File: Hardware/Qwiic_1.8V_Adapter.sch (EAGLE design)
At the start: 18 parts, among them J1 QWIIC_RIGHT_ANGLE, J2 QWIIC_RIGHT_ANGLE, U3 AP2127K-1.8V

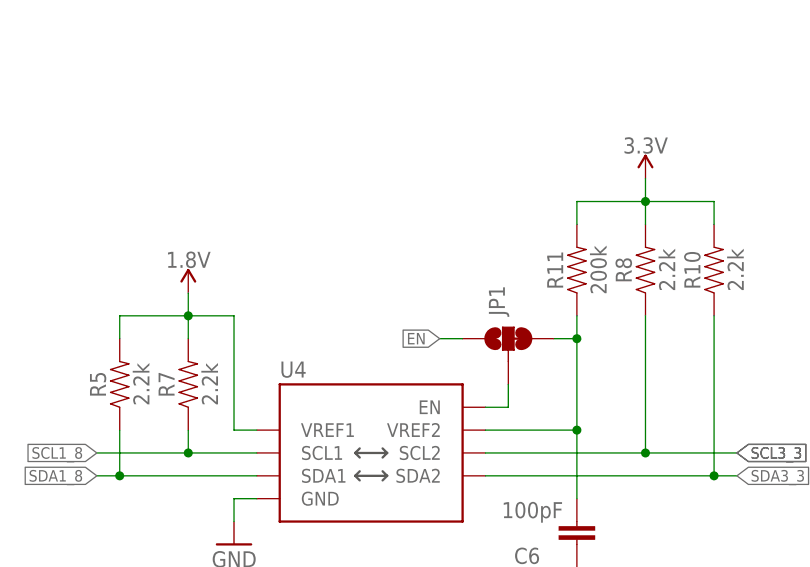
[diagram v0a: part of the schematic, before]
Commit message: Add EN Jumper note
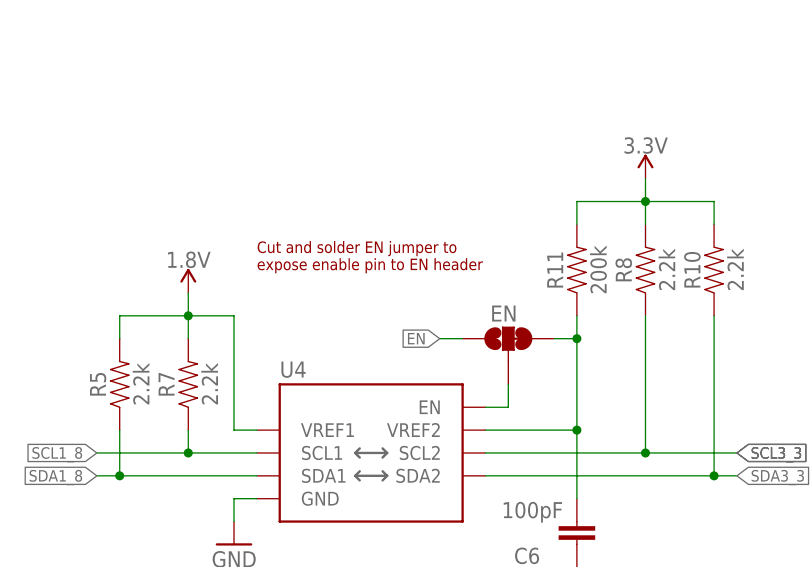
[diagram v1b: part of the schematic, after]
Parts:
- renumbered JP1 to EN
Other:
- note added: "Cut and solder EN jumper to expose enable pin to EN header"
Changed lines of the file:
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@@
 <part name="J4" library="SparkFun-Connectors" deviceset="CONN_05" device="NO_SILK"/>
 <part name="J5" library="SparkFun-Connectors" deviceset="CONN_04" device="1X04_NO_SILK"/>
-<part name="JP1" library="SparkFun-Jumpers" deviceset="JUMPER-SMT_3_1-NC_TRACE" device="_SILK" package3d_urn="urn:adsk.eagle:package:39288/1"/>
+<part name="EN" library="SparkFun-Jumpers" deviceset="JUMPER-SMT_3_1-NC_TRACE" device="_SILK" package3d_urn="urn:adsk.eagle:package:39288/1"/>
 <part name="SUPPLY4" library="SparkFun-PowerSymbols" deviceset="3.3V" device=""/>
 <part name="GND1" library="SparkFun-PowerSymbols" deviceset="GND" device=""/>
@@
 <text x="149.86" y="106.68" size="2.54" layer="97">Qwiic Connectors</text>
 <text x="149.86" y="68.58" size="2.54" layer="97">0.1" Headers</text>
+<text x="55.88" y="111.76" size="1.27" layer="94">Cut and solder EN jumper to
+expose enable pin to EN header</text>
 </plain>
 <instances>
@@
 <attribute name="NAME" x="205.74" y="58.928" size="1.778" layer="95" font="vector"/>
 </instance>
-<instance part="JP1" gate="G$1" x="83.82" y="104.14" smashed="yes" rot="R90">
-<attribute name="NAME" x="83.439" y="106.68" size="1.778" layer="95" font="vector" rot="R90"/>
+<instance part="EN" gate="G$1" x="83.82" y="104.14" smashed="yes" rot="R90">
+<attribute name="NAME" x="84.836" y="107.823" size="1.778" layer="95" font="vector" rot="R180"/>
 </instance>
 <instance part="SUPPLY4" gate="G$1" x="185.42" y="99.06" smashed="yes">
@@
 <wire x1="91.44" y1="93.98" x2="91.44" y2="86.36" width="0.1524" layer="91"/>
 <junction x="91.44" y="93.98"/>
-<pinref part="JP1" gate="G$1" pin="3"/>
+<pinref part="EN" gate="G$1" pin="3"/>
 <wire x1="88.9" y1="104.14" x2="91.44" y2="104.14" width="0.1524" layer="91"/>
 <junction x="91.44" y="104.14"/>
@@
 <segment>
 <pinref part="U4" gate="G$1" pin="EN"/>
-<pinref part="JP1" gate="G$1" pin="2"/>
+<pinref part="EN" gate="G$1" pin="2"/>
 <wire x1="81.28" y1="96.52" x2="83.82" y2="96.52" width="0.1524" layer="91"/>
 <wire x1="83.82" y1="96.52" x2="83.82" y2="99.06" width="0.1524" layer="91"/>
@@
 <net name="EN" class="0">
 <segment>
-<pinref part="JP1" gate="G$1" pin="1"/>
+<pinref part="EN" gate="G$1" pin="1"/>
 <wire x1="78.74" y1="104.14" x2="76.2" y2="104.14" width="0.1524" layer="91"/>
 <label x="76.2" y="104.14" size="1.27" layer="95" rot="R180" xref="yes"/>
@@
 </drawing>
 <compatibility>
+<note version="6.3" minversion="6.2.2" severity="warning">
+Since Version 6.2.2 text objects can contain more than one line,
+which will not be processed correctly with this version.
+</note>
 <note version="8.3" severity="warning">
 Since Version 8.3, EAGLE supports URNs for individual library

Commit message: Production Files and README
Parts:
- added JP1: JUMPER-SMT_2_NC_TRACE_SILK, SparkFun-Jumpers:JUMPER-SMT_2_NC_TRACE_SILK
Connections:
- new net N$3: JP1.1, R1.1
- net 3.3V: now also JP1.2; no longer R1.1
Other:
- moved on the sheet: D1, R1
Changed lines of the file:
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@@
 <part name="GND5" library="SparkFun-PowerSymbols" deviceset="GND" device=""/>
 <part name="SUPPLY9" library="SparkFun-PowerSymbols" deviceset="3.3V" device=""/>
+<part name="JP1" library="SparkFun-Jumpers" deviceset="JUMPER-SMT_2_NC_TRACE" device="_SILK" package3d_urn="urn:adsk.eagle:package:39281/1"/>
 </parts>
 <sheets>
@@
 <attribute name="VALUE" x="218.44" y="61.214" size="1.778" layer="96" align="bottom-center"/>
 </instance>
-<instance part="D1" gate="G$1" x="231.14" y="142.24" smashed="yes">
-<attribute name="NAME" x="227.711" y="137.668" size="1.778" layer="95" font="vector" rot="R90"/>
-<attribute name="VALUE" x="233.045" y="137.668" size="1.778" layer="96" font="vector" rot="R90" align="top-left"/>
-</instance>
-<instance part="R1" gate="G$1" x="231.14" y="152.4" smashed="yes" rot="R270">
-<attribute name="NAME" x="232.664" y="152.4" size="1.778" layer="95" font="vector" rot="R270" align="bottom-center"/>
-<attribute name="VALUE" x="229.616" y="152.4" size="1.778" layer="96" font="vector" rot="R270" align="top-center"/>
-</instance>
-<instance part="GND5" gate="1" x="231.14" y="132.08" smashed="yes">
-<attribute name="VALUE" x="231.14" y="131.826" size="1.778" layer="96" align="top-center"/>
-</instance>
-<instance part="SUPPLY9" gate="G$1" x="231.14" y="160.02" smashed="yes">
-<attribute name="VALUE" x="231.14" y="162.814" size="1.778" layer="96" align="bottom-center"/>
+<instance part="D1" gate="G$1" x="231.14" y="134.62" smashed="yes">
+<attribute name="NAME" x="227.711" y="130.048" size="1.778" layer="95" font="vector" rot="R90"/>
+<attribute name="VALUE" x="233.045" y="130.048" size="1.778" layer="96" font="vector" rot="R90" align="top-left"/>
+</instance>
+<instance part="R1" gate="G$1" x="231.14" y="144.78" smashed="yes" rot="R270">
+<attribute name="NAME" x="232.664" y="144.78" size="1.778" layer="95" font="vector" rot="R270" align="bottom-center"/>
+<attribute name="VALUE" x="229.616" y="144.78" size="1.778" layer="96" font="vector" rot="R270" align="top-center"/>
+</instance>
+<instance part="GND5" gate="1" x="231.14" y="124.46" smashed="yes">
+<attribute name="VALUE" x="231.14" y="124.206" size="1.778" layer="96" align="top-center"/>
+</instance>
+<instance part="SUPPLY9" gate="G$1" x="231.14" y="165.1" smashed="yes">
+<attribute name="VALUE" x="231.14" y="167.894" size="1.778" layer="96" align="bottom-center"/>
+</instance>
+<instance part="JP1" gate="G$1" x="231.14" y="157.48" smashed="yes" rot="R90">
+<attribute name="NAME" x="228.6" y="154.94" size="1.778" layer="95" font="vector" rot="R90"/>
 </instance>
 </instances>
@@
 <pinref part="D1" gate="G$1" pin="C"/>
 <pinref part="GND5" gate="1" pin="GND"/>
-<wire x1="231.14" y1="137.16" x2="231.14" y2="134.62" width="0.1524" layer="91"/>
+<wire x1="231.14" y1="129.54" x2="231.14" y2="127" width="0.1524" layer="91"/>
 </segment>
 </net>
@@
 </segment>
 <segment>
+<pinref part="JP1" gate="G$1" pin="2"/>
 <pinref part="SUPPLY9" gate="G$1" pin="3.3V"/>
-<pinref part="R1" gate="G$1" pin="1"/>
-<wire x1="231.14" y1="160.02" x2="231.14" y2="157.48" width="0.1524" layer="91"/>
+<wire x1="231.14" y1="162.56" x2="231.14" y2="165.1" width="0.1524" layer="91"/>
 </segment>
 </net>
@@
 <pinref part="R1" gate="G$1" pin="2"/>
 <pinref part="D1" gate="G$1" pin="A"/>
-<wire x1="231.14" y1="147.32" x2="231.14" y2="144.78" width="0.1524" layer="91"/>
-</segment>
-</net>
+<wire x1="231.14" y1="139.7" x2="231.14" y2="137.16" width="0.1524" layer="91"/>
+</segment>
+</net>
+<net name="N$3" class="0">
+<segment>
+<pinref part="R1" gate="G$1" pin="1"/>
+<pinref part="JP1" gate="G$1" pin="1"/>
+<wire x1="231.14" y1="149.86" x2="231.14" y2="152.4" width="0.1524" layer="91"/>
+</segment>
+</net>
